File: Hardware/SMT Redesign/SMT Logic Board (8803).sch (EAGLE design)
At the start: 32 parts, among them J4 KLDX-0202-B, SW1 FSMRA4JH04, SW2 FSMRA4JH04, SW3 5MS1S102AM6QES, U1 TLV76750QWDRBRQ1, U2 1364-HVPS-H, U3 PIC16F18444-E/GZ, U5 RV-8803-C7

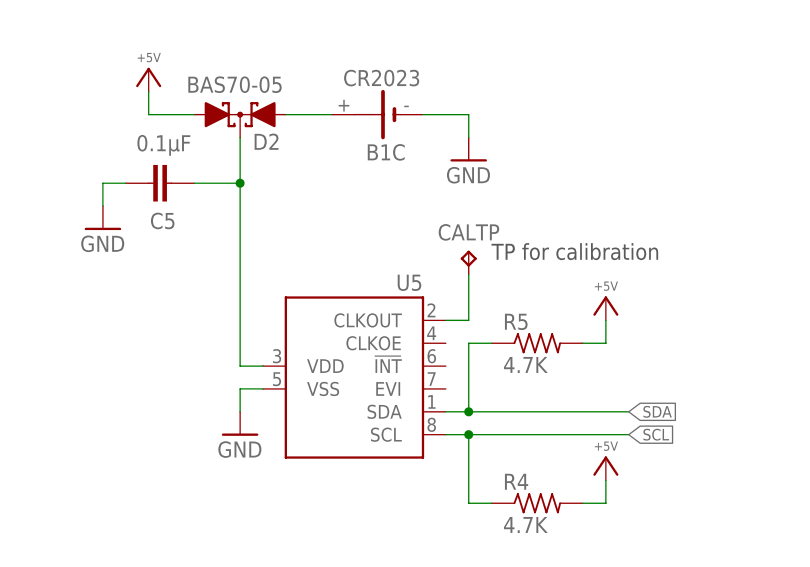
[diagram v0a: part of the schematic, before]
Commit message: Component numbering fix
There was a gap from U3 to U5, shifted U5 onwards down one (eg to U4).

Was also playing the with DR for JLCPCB, some pads etc may be wonky because of this.
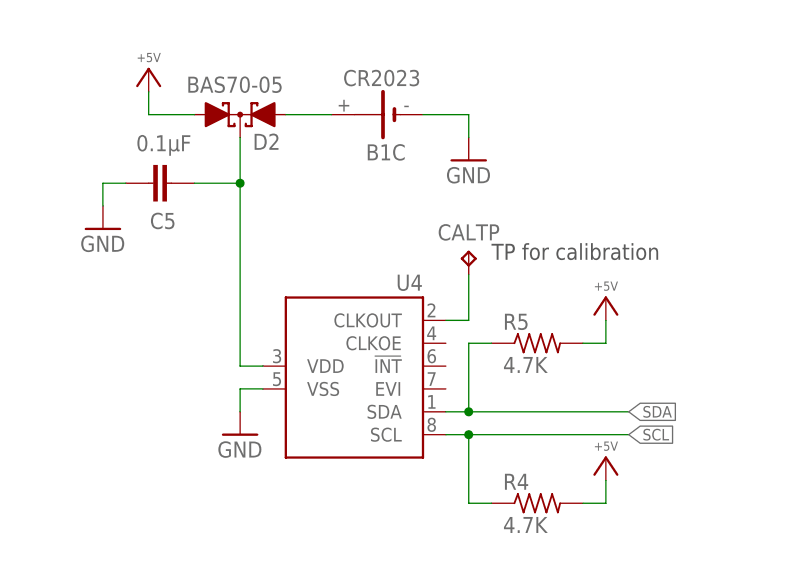
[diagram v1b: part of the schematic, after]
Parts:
- renumbered U5 to U4
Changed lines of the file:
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@@
 <part name="C5" library="My Imported Components" library_urn="urn:adsk.eagle:library:29231634" deviceset="C-EU" device="" package3d_urn="urn:adsk.eagle:package:29231716/2" value="0.1µF"/>
 <part name="P+1" library="supply1" library_urn="urn:adsk.eagle:library:371" deviceset="+5V" device=""/>
-<part name="U5" library="My Imported Components" library_urn="urn:adsk.eagle:library:29231634" deviceset="RV-8803-C7" device="" package3d_urn="urn:adsk.eagle:package:29231763/3"/>
+<part name="U4" library="My Imported Components" library_urn="urn:adsk.eagle:library:29231634" deviceset="RV-8803-C7" device="" package3d_urn="urn:adsk.eagle:package:29231763/3"/>
 <part name="D2" library="My Imported Components" library_urn="urn:adsk.eagle:library:29231634" deviceset="BAS70-05" device="" package3d_urn="urn:adsk.eagle:package:29330405/3"/>
 <part name="CALTP" library="testpad" library_urn="urn:adsk.eagle:library:385" deviceset="TP" device="TP18R" package3d_urn="urn:adsk.eagle:package:27981/1" override_package3d_urn="urn:adsk.eagle:package:29359131/3" override_package_urn="urn:adsk.eagle:footprint:27927/1"/>
@@
 <attribute name="VALUE" x="25.4" y="196.342" size="1.016" layer="96" rot="R180" align="top-center"/>
 </instance>
-<instance part="U5" gate="G$1" x="40.64" y="152.4" smashed="yes">
+<instance part="U4" gate="G$1" x="40.64" y="152.4" smashed="yes">
 <attribute name="NAME" x="55.88" y="172.72" size="1.778" layer="95" rot="R180"/>
 </instance>
@@
 </segment>
 <segment>
-<pinref part="U5" gate="G$1" pin="VSS"/>
+<pinref part="U4" gate="G$1" pin="VSS"/>
 <pinref part="SUPPLY7" gate="1" pin="GND"/>
 <wire x1="38.1" y1="160.02" x2="35.56" y2="160.02" width="0.1524" layer="91"/>
@@
 <wire x1="58.42" y1="157.48" x2="60.96" y2="157.48" width="0.1524" layer="91"/>
 <pinref part="R5" gate="G$1" pin="1"/>
-<pinref part="U5" gate="G$1" pin="SDA"/>
+<pinref part="U4" gate="G$1" pin="SDA"/>
 <wire x1="60.96" y1="157.48" x2="78.74" y2="157.48" width="0.1524" layer="91"/>
 <label x="78.74" y="157.48" size="1.27" layer="95" xref="yes"/>
@@
 <wire x1="58.42" y1="154.94" x2="60.96" y2="154.94" width="0.1524" layer="91"/>
 <pinref part="R4" gate="G$1" pin="1"/>
-<pinref part="U5" gate="G$1" pin="SCL"/>
+<pinref part="U4" gate="G$1" pin="SCL"/>
 <wire x1="60.96" y1="154.94" x2="78.74" y2="154.94" width="0.1524" layer="91"/>
 <wire x1="63.5" y1="147.32" x2="60.96" y2="147.32" width="0.1524" layer="91"/>
@@
 <pinref part="C5" gate="G$1" pin="1"/>
 <wire x1="35.56" y1="182.88" x2="30.48" y2="182.88" width="0.1524" layer="91"/>
-<pinref part="U5" gate="G$1" pin="VDD"/>
+<pinref part="U4" gate="G$1" pin="VDD"/>
 <pinref part="D2" gate="G$1" pin="C"/>
 <wire x1="35.56" y1="187.96" x2="35.56" y2="182.88" width="0.1524" layer="91"/>
@@
 <net name="CLKTEST" class="0">
 <segment>
-<pinref part="U5" gate="G$1" pin="CLKOUT"/>
+<pinref part="U4" gate="G$1" pin="CLKOUT"/>
 <pinref part="CALTP" gate="G$1" pin="TP"/>
 <wire x1="58.42" y1="167.64" x2="60.96" y2="167.64" width="0.1524" layer="91"/>
